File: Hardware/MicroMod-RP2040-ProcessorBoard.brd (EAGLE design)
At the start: 22 x 22 mm, 48 parts, among them J1 MICROMOD-2222, U1 W25QXX128MBIT, U3 RP2040, Y1 12MHz

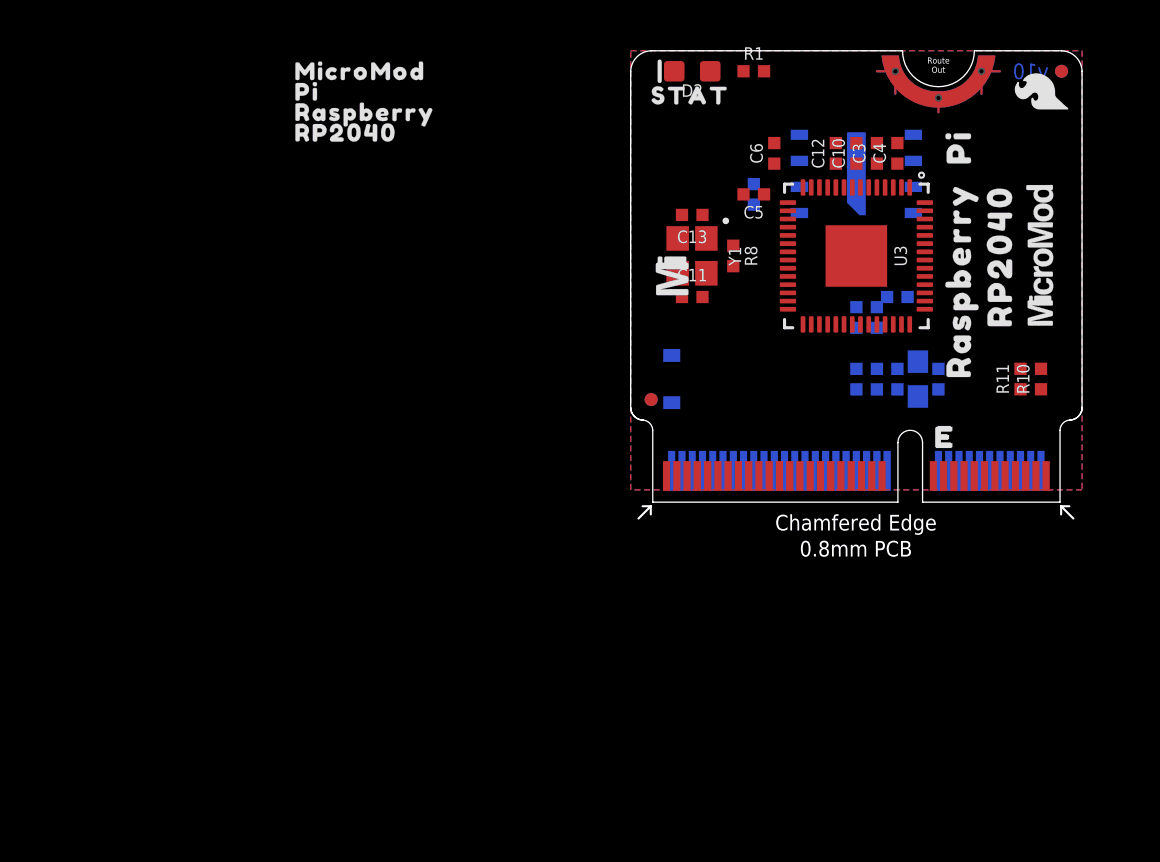
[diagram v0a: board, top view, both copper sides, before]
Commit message: Add pullup to flash
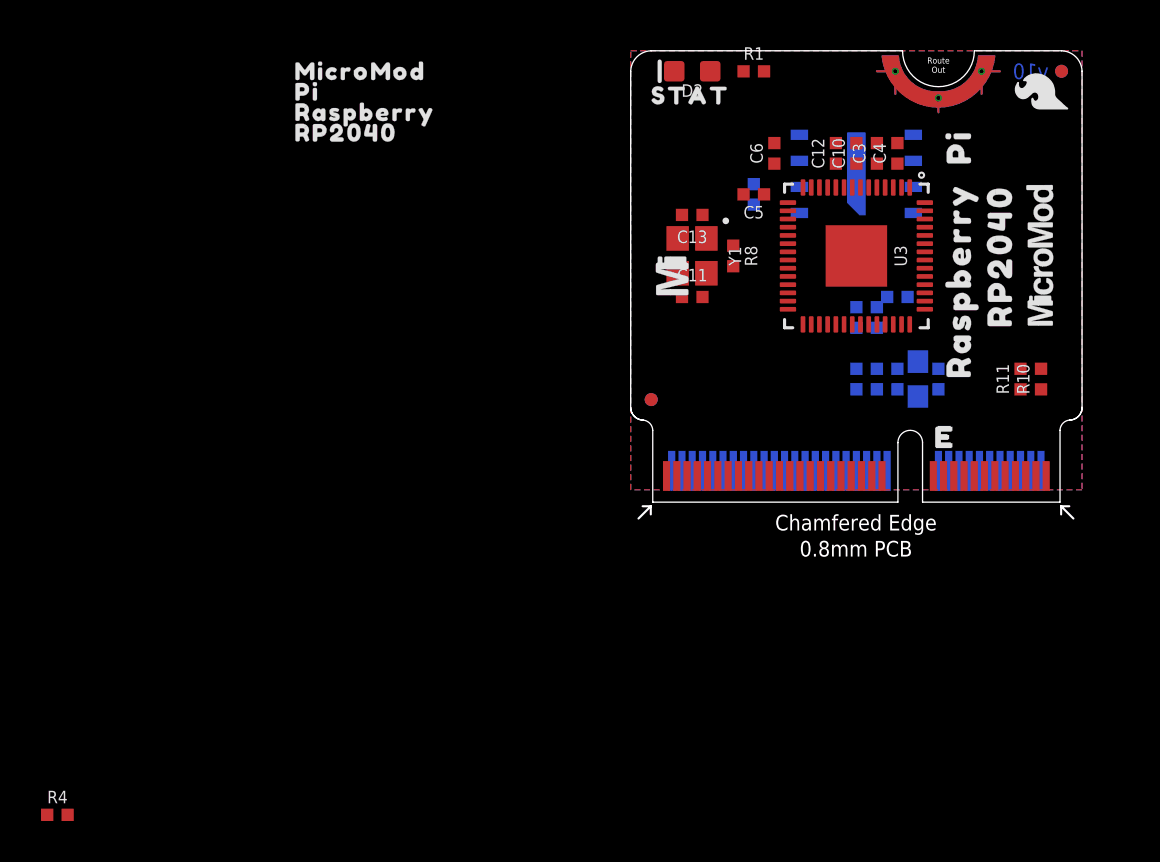
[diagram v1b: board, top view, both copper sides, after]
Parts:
- removed D7: 1A/23V/620mV, SparkFun-DiscreteSemi:SOD-323
- added R4: 10k, SparkFun-Resistors:0402-TIGHT
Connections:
- removed net 3.3V_NOBATT: C15.1, C29.1, D7.A, J1.2, J1.74, U1.8
- net 3.3V: now also C15.1, C29.1, J1.2, J1.74, R4.2, U1.8; no longer D7.C
- net QSPI-CS: now also R4.1
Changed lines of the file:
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@@
 <element name="U$10" library="output" package="_RASPBERRY1" value="" x="16" y="10.6" smashed="yes" rot="R90"/>
 <element name="U$12" library="SparkFun-MicroMod" package="MICROMOD_LOGO_.3" value="" x="20" y="12" smashed="yes" rot="R90"/>
-<element name="D7" library="SparkFun-DiscreteSemi" package="SOD-323" value="1A/23V/620mV" x="2" y="6" smashed="yes" rot="MR270">
-<attribute name="NAME" x="1.238" y="6" size="0.6096" layer="26" font="vector" ratio="20" rot="MR270" align="bottom-center"/>
-<attribute name="PROD_ID" value="DIO-11623" x="2" y="7" size="1.778" layer="28" font="vector" ratio="15" rot="MR270" display="off"/>
-<attribute name="VALUE" x="2.762" y="6" size="0.6096" layer="28" font="vector" ratio="20" rot="MR270" align="top-center"/>
+<element name="R4" library="SparkFun-Resistors" package="0402-TIGHT" value="10k" x="-27.94" y="-15.24" smashed="yes">
+<attribute name="NAME" x="-27.94" y="-14.678" size="0.6096" layer="25" font="vector" ratio="20" align="bottom-center"/>
+<attribute name="PROD_ID" value="RES-14241" x="-27.94" y="-15.24" size="1.778" layer="27" font="vector" ratio="15" display="off"/>
+<attribute name="VALUE" x="-27.94" y="-15.802" size="0.6096" layer="27" font="vector" ratio="20" align="top-center"/>
 </element>
 </elements>
@@
 <contactref element="R2" pad="2"/>
 <contactref element="J1" pad="72"/>
-<contactref element="D7" pad="C"/>
+<contactref element="J1" pad="2"/>
+<contactref element="J1" pad="74"/>
+<contactref element="R4" pad="2"/>
+<contactref element="C29" pad="1"/>
+<contactref element="U1" pad="8"/>
+<contactref element="C15" pad="1"/>
+<wire x1="2" y1="1.525" x2="-27.44" y2="-15.24" width="0" layer="19" extent="1-16"/>
+<wire x1="2.5" y1="1.525" x2="2" y2="1.525" width="0" layer="19" extent="16-16"/>
+<wire x1="11" y1="6.5" x2="2.5" y2="1.525" width="0" layer="19" extent="16-16"/>
+<wire x1="12" y1="6.5" x2="11" y2="6.5" width="0" layer="19" extent="16-16"/>
+<wire x1="13" y1="6.5" x2="12" y2="6.5" width="0" layer="19" extent="16-16"/>
+<wire x1="14" y1="5.15" x2="13" y2="6.5" width="0" layer="19" extent="16-16"/>
+<wire x1="11" y1="8.5" x2="11" y2="6.5" width="0" layer="19" extent="16-16"/>
+<wire x1="10" y1="8.6635" x2="11" y2="8.5" width="0" layer="19" extent="1-16"/>
+<wire x1="13.6" y1="8.6635" x2="13" y2="6.5" width="0" layer="19" extent="1-16"/>
+<wire x1="13.5" y1="10" x2="13.6" y2="8.6635" width="0" layer="19" extent="1-16"/>
+<wire x1="14.3365" y1="9.8" x2="13.5" y2="10" width="0" layer="19" extent="1-16"/>
+<wire x1="14.3365" y1="11.4" x2="14.3365" y2="9.8" width="0" layer="19" extent="1-1"/>
+<wire x1="14.3365" y1="11.8" x2="14.3365" y2="11.4" width="0" layer="19" extent="1-1"/>
+<wire x1="13.775" y1="14.095" x2="14.3365" y2="11.8" width="0" layer="19" extent="1-16"/>
+<wire x1="13.6" y1="15.3365" x2="13.775" y2="14.095" width="0" layer="19" extent="1-16"/>
 <wire x1="13" y1="16.5" x2="13.6" y2="15.3365" width="0" layer="19" extent="1-1"/>
 <wire x1="11" y1="16.5" x2="13" y2="16.5" width="0" layer="19" extent="1-1"/>
@@
 <wire x1="6.5" y1="15" x2="7" y2="16.5" width="0" layer="19" extent="1-1"/>
 <wire x1="7.6635" y1="11.8" x2="6.5" y2="15" width="0" layer="19" extent="1-1"/>
-<wire x1="14.3365" y1="11.8" x2="13.6" y2="15.3365" width="0" layer="19" extent="1-1"/>
-<wire x1="14.3365" y1="11.4" x2="14.3365" y2="11.8" width="0" layer="19" extent="1-1"/>
-<wire x1="14.3365" y1="9.8" x2="14.3365" y2="11.4" width="0" layer="19" extent="1-1"/>
-<wire x1="13.5" y1="10" x2="14.3365" y2="9.8" width="0" layer="19" extent="1-16"/>
-<wire x1="13.6" y1="8.6635" x2="14.3365" y2="9.8" width="0" layer="19" extent="1-1"/>
-<wire x1="11" y1="8.5" x2="13.6" y2="8.6635" width="0" layer="19" extent="1-16"/>
-<wire x1="10" y1="8.6635" x2="11" y2="8.5" width="0" layer="19" extent="1-16"/>
-<wire x1="11" y1="6.5" x2="11" y2="8.5" width="0" layer="19" extent="16-16"/>
-<wire x1="14" y1="5.15" x2="11" y2="6.5" width="0" layer="19" extent="16-16"/>
-<wire x1="2" y1="7.15" x2="7.6635" y2="11.8" width="0" layer="19" extent="1-16"/>
-<wire x1="2.5" y1="1.525" x2="2" y2="7.15" width="0" layer="19" extent="16-16"/>
+<wire x1="20" y1="1.525" x2="14" y2="5.15" width="0" layer="19" extent="16-16"/>
 </signal>
 <signal name="QSPI-CS">
@@
 <contactref element="U1" pad="1"/>
 <contactref element="R9" pad="1"/>
-<wire x1="8.225" y1="14.095" x2="14.3365" y2="14.6" width="0" layer="19" extent="1-16"/>
-<wire x1="6" y1="14.5" x2="8.225" y2="14.095" width="0" layer="19" extent="16-16"/>
+<contactref element="R4" pad="1"/>
+<wire x1="6" y1="14.5" x2="-28.44" y2="-15.24" width="0" layer="19" extent="1-16"/>
+<wire x1="8.225" y1="14.095" x2="6" y2="14.5" width="0" layer="19" extent="16-16"/>
+<wire x1="14.3365" y1="14.6" x2="8.225" y2="14.095" width="0" layer="19" extent="1-16"/>
 </signal>
 <signal name="QSPI-CLK" class="2">
@@
 <wire x1="3.75" y1="1.275" x2="12.8" y2="8.6635" width="0" layer="19" extent="1-1"/>
 </signal>
-<signal name="3.3V_NOBATT">
-<contactref element="J1" pad="2"/>
-<contactref element="J1" pad="74"/>
-<contactref element="D7" pad="A"/>
-<contactref element="C15" pad="1"/>
-<contactref element="C29" pad="1"/>
-<contactref element="U1" pad="8"/>
-<wire x1="13" y1="6.5" x2="13.775" y2="14.095" width="0" layer="19" extent="16-16"/>
-<wire x1="12" y1="6.5" x2="13" y2="6.5" width="0" layer="19" extent="16-16"/>
-<wire x1="20" y1="1.525" x2="13" y2="6.5" width="0" layer="19" extent="16-16"/>
-<wire x1="2" y1="4.85" x2="12" y2="6.5" width="0" layer="19" extent="16-16"/>
-<wire x1="2" y1="1.525" x2="2" y2="4.85" width="0" layer="19" extent="16-16"/>
-</signal>
 </signals>

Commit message: Adding production files
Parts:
- removed U$6: (no value), output:RP20402
- added C2: 0.1uF, SparkFun-Capacitors:0402-TIGHT
- added R18: 1k, SparkFun-Resistors:0402-TIGHT
- added R5: 10k, SparkFun-Resistors:0402-TIGHT
- added U2: FSUSB30MUX_MSOP10, RP2040:MSOP10
- R2: value 200 -> 200OHM-0402T-1/16W-1%; device SparkFun-Resistors:0603 -> SparkFun-Resistors:0402-TIGHT
- U$2: device output:MICROMOD3 -> output:PI2
- U$3: device output:PI1 -> SparkFun-MicroMod:MICROMOD_LOGO_.3
- U$4: device output:RASPBERRY0 -> output:RP20400
- U$5: device SparkFun-MicroMod:MICROMOD_LOGO_.35 -> output:_RASPBERRY1
- moved R4 44.7 mm to (5.00, 15.0), flipped to the bottom, turned to 90 degrees
- moved U$2 27.9 mm to (7.20, 7.10), flipped to the bottom, turned to 90 degrees
- moved U$7 27.1 mm to (5.00, 20.0)
- moved U$4 25.6 mm to (5.70, 7.10), flipped to the bottom, turned to 90 degrees
- moved U$3 24.7 mm to (4.00, 7.00), flipped to the bottom, turned to 90 degrees
- moved U$5 17.6 mm to (8.90, 7.30), turned to 90 degrees
- moved LOGO1 11.0 mm to (1.70, 11.2), turned to 90 degrees
- moved C15 10.8 mm to (16.0, 16.0), turned to 90 degrees
- moved C29 10.2 mm to (15.0, 16.0), turned to 90 degrees
- moved C12 9.22 mm to (16.0, 10.0), flipped to the bottom, turned to 180 degrees
- moved R10 7.21 mm to (16.0, 12.0), flipped to the bottom, turned to 0 degrees
- moved C10 6.40 mm to (16.0, 13.0), flipped to the bottom, turned to 180 degrees
- moved C14 6.32 mm to (6.00, 11.0), turned to 0 degrees
- moved R11 5.83 mm to (16.0, 11.0), flipped to the bottom, turned to 0 degrees
- moved C3 5.00 mm to (16.0, 14.0), flipped to the bottom, turned to 180 degrees
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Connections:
- net N$1 renamed RP_D1-
- net N$3 renamed ADC_VDD
- net N$7 renamed RP_D1+
- removed net GPIO8: J1.67, U3.40
- removed net I2C_!INT!: J1.16, U3.16
- removed net LED_BUILTIN: R1.2, U3.37
- removed net SPI_!CS1!/SDIO_DAT3: J1.70, U3.12
- new net GPIO9: J1.65, U3.40
- new net I2C_!INT!/TX2: J1.16, J1.22, U3.11
- new net LED_BUILTIN/G10: J1.63, R1.2, U3.37
- new net RP_D+: R10.1, U2.4
- new net RP_D-: R11.1, U2.6
- new net SPI_!CS1!/SDIO_DAT3/RX2: J1.20, J1.70, U3.12
- new net USBHOST_D+: J1.35, U2.2
- new net USBHOST_D-: J1.37, U2.8
- new net USB_MUX_SIG: R18.2, R5.2, U2.1
- new net USB_VIN: J1.9, R18.1
- net 3.3V: now also C2.1, U2.10
- net GND: now also C2.2, R5.1, U2.5, U2.9
- net PWM0: now also U3.16; no longer U3.11
- net USB_D+: now also U2.3; no longer J1.35, R10.1
- net USB_D-: now also U2.7; no longer J1.37, R11.1
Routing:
- net SPI_!CS1!/SDIO_DAT3/RX2: track 0.00 -> 45.6 mm, vias 0 -> 4
- net LED_BUILTIN/G10: track 0.00 -> 40.6 mm, vias 0 -> 4
- net 3.3V: track 0.00 -> 36.7 mm, vias 0 -> 13
- net SDIO_DAT1/AUD_IN: track 0.00 -> 36.1 mm, vias 0 -> 6
- net CTS1/AUD_LRCLK: track 0.00 -> 35.7 mm, vias 0 -> 4
- net I2C_!INT!/TX2: track 0.00 -> 34.9 mm, vias 0 -> 3
- net RTS1/AUD_BCLK: track 0.00 -> 34.8 mm, vias 0 -> 4
- net SDIO_DAT2/AUD_OUT: track 0.00 -> 33.3 mm, vias 0 -> 4
- net D0: track 0.00 -> 31.5 mm, vias 0 -> 3
- net PWM0: track 0.00 -> 30.4 mm, vias 0 -> 3
- net BOOT: track 0.00 -> 28.4 mm, vias 0 -> 3
- net SDA: track 0.00 -> 27.7 mm, vias 0 -> 3
- net SCL: track 0.00 -> 27.5 mm, vias 0 -> 3
- net D1: track 0.00 -> 25.0 mm, vias 0 -> 3
- net !RESET!: track 0.00 -> 23.9 mm, vias 0 -> 3
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- added copper zone on layer 15, net 3.3V
- removed copper zone on layer 15, net V_BATT

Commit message: Update USB mux prod ID
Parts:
- U2: device RP2040:MSOP10 -> SparkFun-IC-Special-Function:MSOP10
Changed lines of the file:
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@@
 <attribute name="VALUE" x="4.438" y="15" size="0.6096" layer="28" font="vector" ratio="20" rot="MR90" align="top-center"/>
 </element>
-<element name="U2" library="RP2040" package="MSOP10" value="FSUSB30MUX_MSOP10" x="19" y="10" smashed="yes" rot="MR270">
+<element name="U2" library="SparkFun-IC-Special-Function" package="MSOP10" value="FSUSB30MUX_MSOP10" x="19" y="10" smashed="yes" rot="MR270">
 <attribute name="NAME" x="17.095" y="10" size="0.6096" layer="26" font="vector" ratio="20" rot="MR270" align="bottom-center"/>
-<attribute name="PROD_ID" value="IC-14135" x="19" y="10" size="1.778" layer="28" font="vector" ratio="15" rot="MR270" display="off"/>
+<attribute name="PROD_ID" value="IC-15569" x="19" y="10" size="1.778" layer="28" font="vector" ratio="15" rot="MR270" display="off"/>
 <attribute name="VALUE" x="21.54" y="10" size="0.6096" layer="28" font="vector" ratio="20" rot="MR270" align="bottom-center"/>
 </element>
@@
 <via x="11" y="13.3" extent="1-16" drill="0.2"/>
 <via x="20.2" y="6" extent="1-16" drill="0.2"/>
+<wire x1="15" y1="19.7" x2="17.1" y2="21" width="0" layer="19" extent="1-1"/>
+<wire x1="14.7" y1="17.5" x2="15" y2="19.7" width="0" layer="19" extent="1-1"/>
+<wire x1="14" y1="17.5" x2="14.7" y2="17.5" width="0" layer="19" extent="1-1"/>
+<wire x1="15" y1="16.5" x2="14.7" y2="17.5" width="0" layer="19" extent="16-16"/>
+<wire x1="16" y1="16.5" x2="15" y2="16.5" width="0" layer="19" extent="16-16"/>
+<wire x1="16.7" y1="16.6" x2="16" y2="16.5" width="0" layer="19" extent="16-16"/>
+<wire x1="17.5" y1="14.8" x2="16.7" y2="16.6" width="0" layer="19" extent="1-1"/>
+<wire x1="17.5" y1="14" x2="17.5" y2="14.8" width="0" layer="19" extent="16-16"/>
+<wire x1="16.5" y1="14" x2="17.5" y2="14" width="0" layer="19" extent="16-16"/>
+<wire x1="16.5" y1="13" x2="16.5" y2="14" width="0" layer="19" extent="16-16"/>
+<wire x1="17.1" y1="13" x2="16.5" y2="13" width="0" layer="19" extent="16-16"/>
+<wire x1="12.9" y1="21" x2="15" y2="19.7" width="0" layer="19" extent="1-1"/>
+<wire x1="20" y1="12.25" x2="17.1" y2="13" width="0" layer="19" extent="16-16"/>
+<wire x1="20.632" y1="12.255" x2="20" y2="12.25" width="0" layer="19" extent="16-16"/>
+<wire x1="16.5" y1="10" x2="16.5" y2="13" width="0" layer="19" extent="16-16"/>
+<wire x1="17.1" y1="10" x2="16.5" y2="10" width="0" layer="19" extent="16-16"/>
+<wire x1="16.5" y1="9" x2="16.5" y2="10" width="0" layer="19" extent="16-16"/>
+<wire x1="17.1" y1="9" x2="16.5" y2="9" width="0" layer="19" extent="16-16"/>
+<wire x1="18.5" y1="7.75" x2="17.1" y2="9" width="0" layer="19" extent="16-16"/>
+<wire x1="18.6" y1="6.7" x2="18.5" y2="7.75" width="0" layer="19" extent="16-16"/>
+<wire x1="19.5" y1="6" x2="18.6" y2="6.7" width="0" layer="19" extent="16-16"/>
+<wire x1="20.2" y1="6" x2="19.5" y2="6" width="0" layer="19" extent="16-16"/>
+<wire x1="16.8" y1="6.4" x2="18.6" y2="6.7" width="0" layer="19" extent="1-1"/>
+<wire x1="16.5" y1="7" x2="16.8" y2="6.4" width="0" layer="19" extent="16-16"/>
+<wire x1="14.3" y1="6.8" x2="16.5" y2="7" width="0" layer="19" extent="16-16"/>
+<wire x1="13.6" y1="6.2" x2="14.3" y2="6.8" width="0" layer="19" extent="16-16"/>
+<wire x1="18.473" y1="3.365" x2="19.5" y2="6" width="0" layer="19" extent="16-16"/>
+<wire x1="18.75" y1="1.275" x2="18.473" y2="3.365" width="0" layer="19" extent="1-1"/>
+<wire x1="20.25" y1="1.275" x2="18.75" y2="1.275" width="0" layer="19" extent="1-1"/>
+<wire x1="11.8" y1="3.7" x2="13.6" y2="6.2" width="0" layer="19" extent="16-16"/>
+<wire x1="11.5" y1="1.525" x2="11.8" y2="3.7" width="0" layer="19" extent="16-16"/>
+<wire x1="10.75" y1="1.275" x2="11.5" y2="1.525" width="0" layer="19" extent="1-16"/>
+<wire x1="12.25" y1="1.275" x2="11.5" y2="1.525" width="0" layer="19" extent="1-16"/>
+<wire x1="9.25" y1="1.275" x2="10.75" y2="1.275" width="0" layer="19" extent="1-1"/>
+<wire x1="9.3" y1="3" x2="9.25" y2="1.275" width="0" layer="19" extent="1-1"/>
+<wire x1="10" y1="6" x2="11.8" y2="3.7" width="0" layer="19" extent="16-16"/>
+<wire x1="10" y1="17.5" x2="14" y2="17.5" width="0" layer="19" extent="1-1"/>
+<wire x1="10" y1="18.1" x2="10" y2="17.5" width="0" layer="19" extent="1-1"/>
+<wire x1="8.225" y1="17.905" x2="10" y2="18.1" width="0" layer="19" extent="16-16"/>
+<wire x1="7.3" y1="17.9" x2="8.225" y2="17.905" width="0" layer="19" extent="16-16"/>
+<wire x1="9.7" y1="13.3" x2="10" y2="17.5" width="0" layer="19" extent="1-1"/>
+<wire x1="11" y1="13.3" x2="9.7" y2="13.3" width="0" layer="19" extent="1-1"/>
+<wire x1="12.2" y1="13.1" x2="11" y2="13.3" width="0" layer="19" extent="1-1"/>
+<wire x1="12.3" y1="12" x2="12.2" y2="13.1" width="0" layer="19" extent="1-1"/>
+<wire x1="12.3" y1="10.7" x2="12.3" y2="12" width="0" layer="19" extent="1-1"/>
+<wire x1="11" y1="12" x2="11" y2="13.3" width="0" layer="19" extent="1-1"/>
+<wire x1="11" y1="10.8" x2="11" y2="12" width="0" layer="19" extent="1-1"/>
+<wire x1="9.7" y1="10.7" x2="11" y2="10.8" width="0" layer="19" extent="1-1"/>
+<wire x1="9.7" y1="12" x2="9.7" y2="13.3" width="0" layer="19" extent="1-1"/>
+<wire x1="7.5635" y1="13" x2="9.7" y2="13.3" width="0" layer="19" extent="1-1"/>
+<wire x1="6.6" y1="13" x2="7.5635" y2="13" width="0" layer="19" extent="1-1"/>
+<wire x1="5.5" y1="12" x2="6.6" y2="13" width="0" layer="19" extent="16-16"/>
+<wire x1="5.5" y1="11" x2="5.5" y2="12" width="0" layer="19" extent="16-16"/>
+<wire x1="4.8" y1="10.7" x2="5.5" y2="11" width="0" layer="19" extent="16-16"/>
+<wire x1="2.5" y1="10" x2="4.8" y2="10.7" width="0" layer="19" extent="1-1"/>
+<wire x1="1.6" y1="10" x2="2.5" y2="10" width="0" layer="19" extent="1-1"/>
+<wire x1="2.5" y1="14" x2="5.5" y2="12" width="0" layer="19" extent="1-16"/>
+<wire x1="1.7" y1="14" x2="2.5" y2="14" width="0" layer="19" extent="1-1"/>
+<wire x1="2.123" y1="21" x2="7.3" y2="17.9" width="0" layer="19" extent="1-1"/>
+<wire x1="1.75" y1="1.275" x2="9.25" y2="1.275" width="0" layer="19" extent="1-1"/>
+<wire x1="1.5" y1="2.5" x2="1.75" y2="1.275" width="0" layer="19" extent="1-1"/>
 </signal>
 <signal name="!RESET!">
@@
 <wire x1="16.75" y1="7.75" x2="16.5" y2="8" width="0.2032" layer="16"/>
 <wire x1="15.5" y1="9" x2="16.5" y2="8" width="0.2032" layer="16"/>
+<wire x1="14.4365" y1="9.8" x2="14.4365" y2="11.4" width="0" layer="19" extent="1-1"/>
+<wire x1="13.6" y1="8.5635" x2="13.6" y2="9.8" width="0" layer="19" extent="1-1"/>
+<wire x1="20.0913" y1="3.048" x2="18.5" y2="5.3" width="0" layer="19" extent="1-1"/>
+<wire x1="10" y1="15.4365" x2="13.6" y2="15.4365" width="0" layer="19" extent="1-1"/>
+<wire x1="8.4" y1="12" x2="9.1" y2="14.7" width="0" layer="19" extent="1-1"/>
+<wire x1="10" y1="8.5635" x2="13.6" y2="8.5635" width="0" layer="19" extent="1-1"/>
+<wire x1="5" y1="15.5" x2="6.5" y2="12" width="0" layer="19" extent="16-16"/>
+<wire x1="1.6325" y1="3.148" x2="10" y2="7" width="0" layer="19" extent="16-16"/>
 </signal>
 <signal name="QSPI-CS">

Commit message: Update silk
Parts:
- removed U$10, U$5: (no value), output:_RASPBERRY1
- removed U$2, U$8: (no value), output:PI2
- moved LOGO3 17.8 mm to (19.7, 18.7), turned to 90 degrees
- moved U$7 15.3 mm to (19.7, 16.0), turned to 90 degrees
- moved U$4 1.78 mm to (3.94, 6.86)
- moved U$3 1.74 mm to (5.71, 6.73)
- moved U$12 0.83 mm to (19.2, 12.1), turned to 270 degrees
- moved LOGO2 0.65 mm to (19.7, 19.4), turned to 270 degrees
- moved U$9 0.48 mm to (17.5, 11.9), turned to 270 degrees
- moved U$1 0.19 mm to (1.81, 6.97), turned to 270 degrees
- moved U$11 0.13 mm to (0.38, 19.7)
